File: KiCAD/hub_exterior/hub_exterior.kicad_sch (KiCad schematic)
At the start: 21 parts

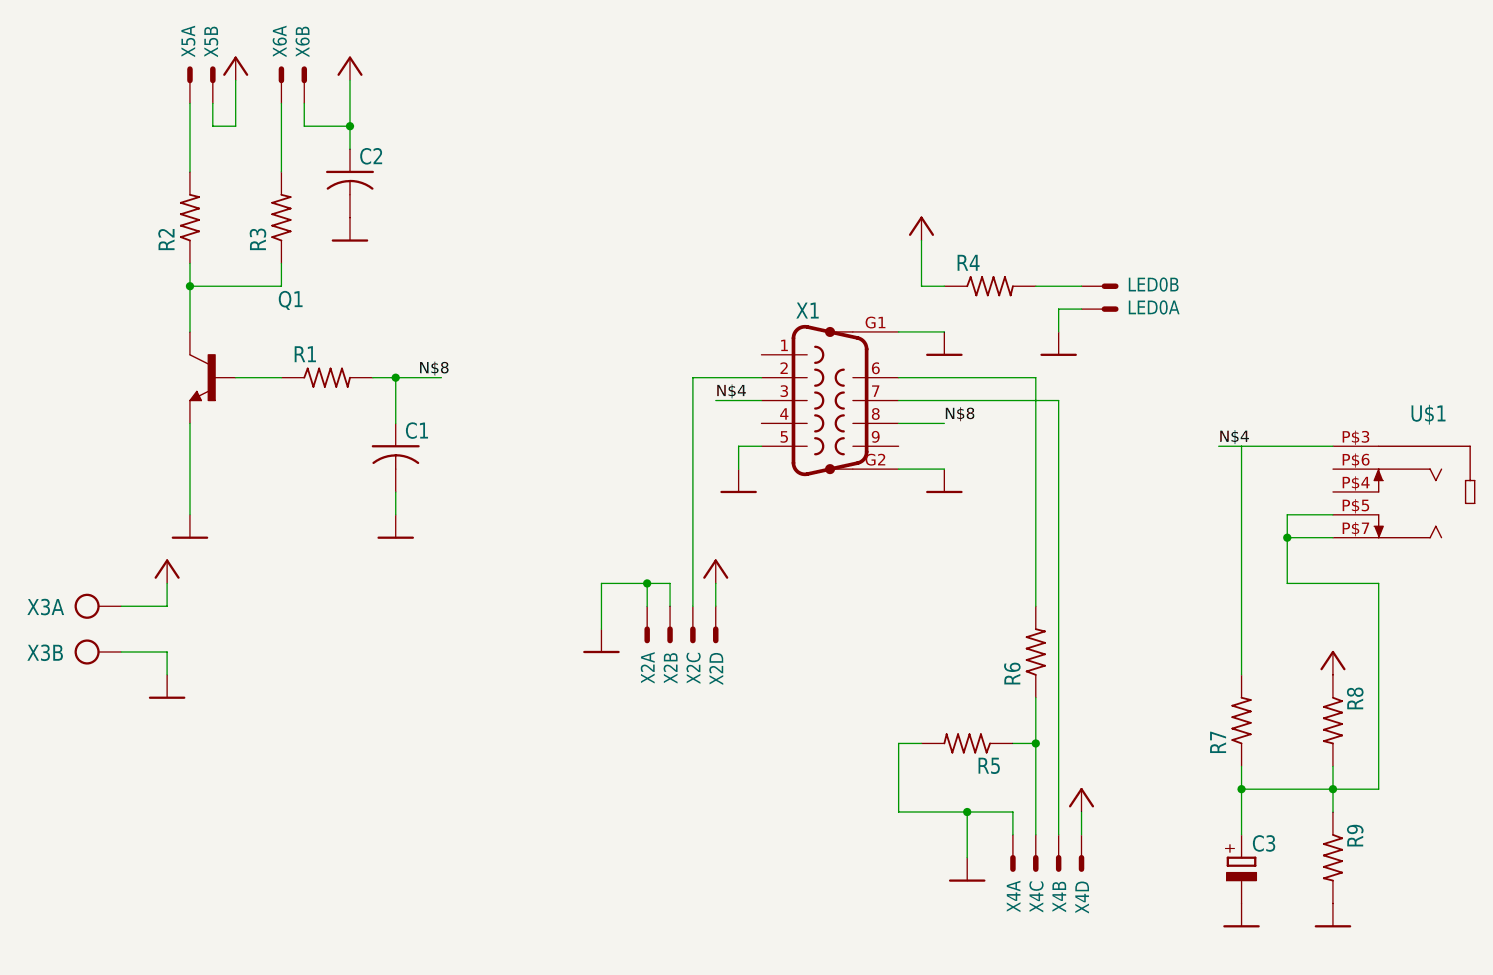
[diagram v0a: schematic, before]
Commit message: rediseño hub exterior
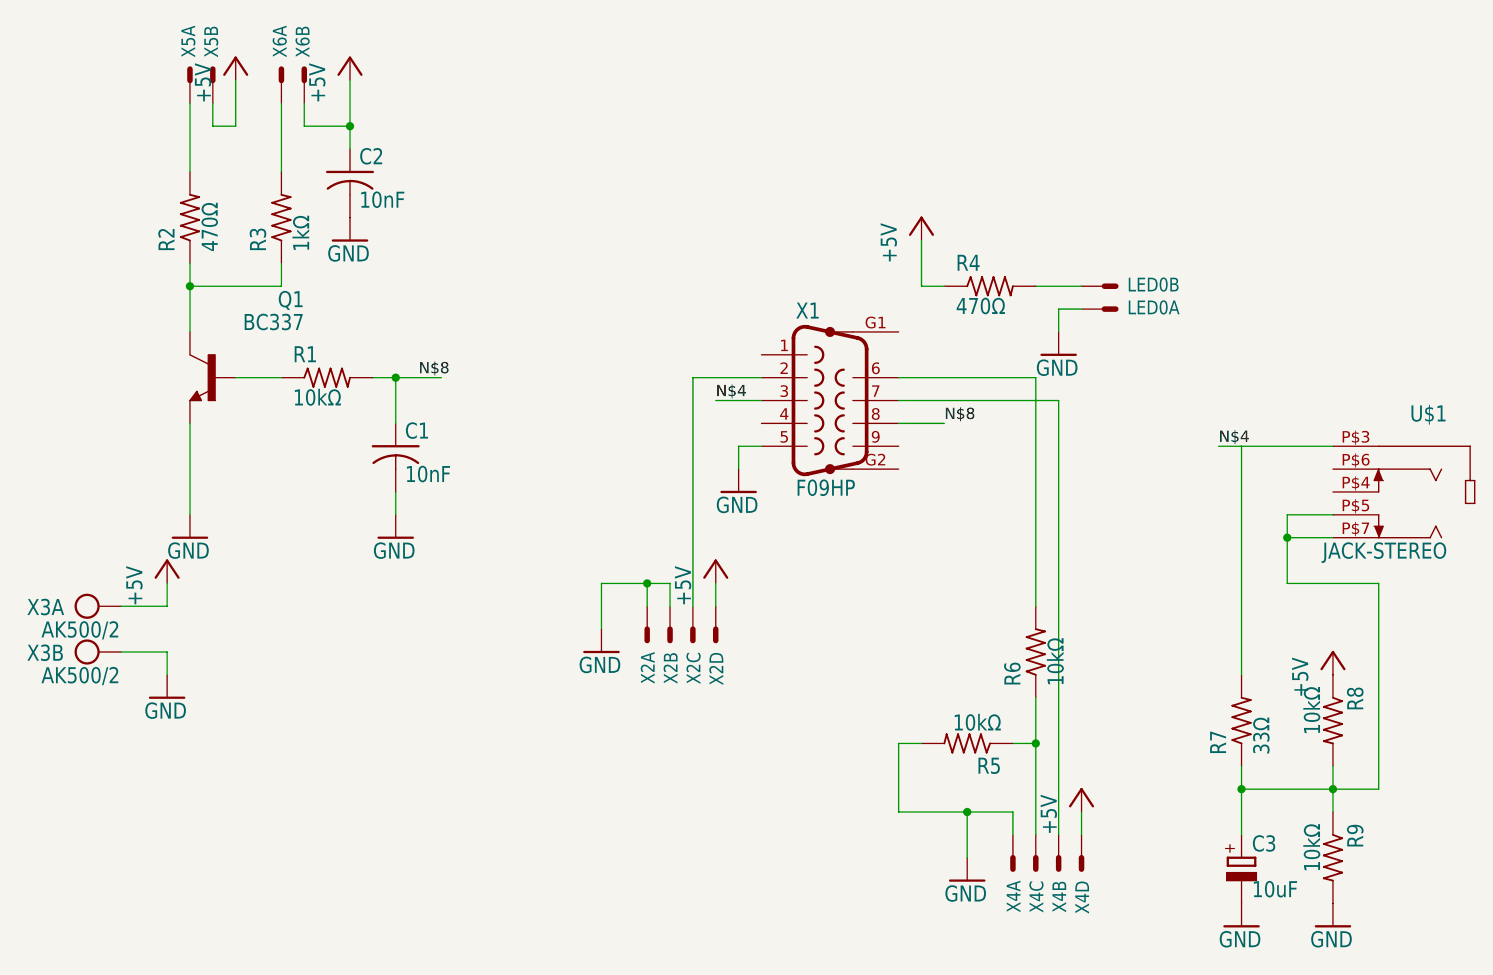
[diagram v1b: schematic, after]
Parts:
- C1, C2: value (none) -> 10nF; footprint (none) -> Capacitor_THT:C_Disc_D7.5mm_W2.5mm_P5.00mm
- C3: value (none) -> 10uF; footprint (none) -> Capacitor_THT:CP_Radial_D5.0mm_P2.50mm
- LED0: value (none) -> LED_VERDE; footprint (none) -> Connector_Molex:Molex_KK-254_AE-6410-02A_1x02_P2.54mm_Vertical
- Q1: value (none) -> BC337; footprint (none) -> Package_TO_SOT_THT:TO-92
- R1, R5, R8, R9: value (none) -> 10kΩ; footprint (none) -> Resistor_THT:R_Axial_DIN0207_L6.3mm_D2.5mm_P7.62mm_Horizontal
- R2, R4: value (none) -> 470Ω; footprint (none) -> Resistor_THT:R_Axial_DIN0207_L6.3mm_D2.5mm_P7.62mm_Horizontal
- R3: value (none) -> 1kΩ; footprint (none) -> Resistor_THT:R_Axial_DIN0207_L6.3mm_D2.5mm_P7.62mm_Horizontal
- R6: value (none) -> 10kΩ; footprint (none) -> Resistor_THT:R_Axial_DIN0207_L6.3mm_D2.5mm_P15.24mm_Horizontal
- R7: value (none) -> 33Ω; footprint (none) -> Resistor_THT:R_Axial_DIN0207_L6.3mm_D2.5mm_P7.62mm_Horizontal
- U$1: value (none) -> JACK-STEREO; footprint (none) -> hub_exterior:SPC21348
- X1: value (none) -> F09HP; footprint (none) -> hub_exterior:F09HP
- X2: value (none) -> LLUVIA; footprint (none) -> Connector_Molex:Molex_KK-254_AE-6410-04A_1x04_P2.54mm_Vertical
- X3: value (none) -> AK500/2; footprint (none) -> TerminalBlock_Phoenix:TerminalBlock_Phoenix_PT-1,5-2-5.0-H_1x02_P5.00mm_Horizontal
- X4: value (none) -> GPS; footprint (none) -> Connector_Molex:Molex_KK-254_AE-6410-04A_1x04_P2.54mm_Vertical
- X5: value (none) -> LED_ROJO; footprint (none) -> Connector_Molex:Molex_KK-254_AE-6410-02A_1x02_P2.54mm_Vertical
- X6: value (none) -> BUZZER; footprint (none) -> Connector_Molex:Molex_KK-254_AE-6410-02A_1x02_P2.54mm_Vertical
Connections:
- net GND: no longer X1.G1, X1.G2
